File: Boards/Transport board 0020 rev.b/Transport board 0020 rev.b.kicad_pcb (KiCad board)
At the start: 2 copper layers, 165.9 x 187.4 mm, 84 parts, among them P1 CEC card edge connector large, U1 TR1602, U10 LM311, U11 LM741, U12 LM311, U13 AH5012, U14 Spare, U15 Spare, U2 6821, U3 DM8602N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

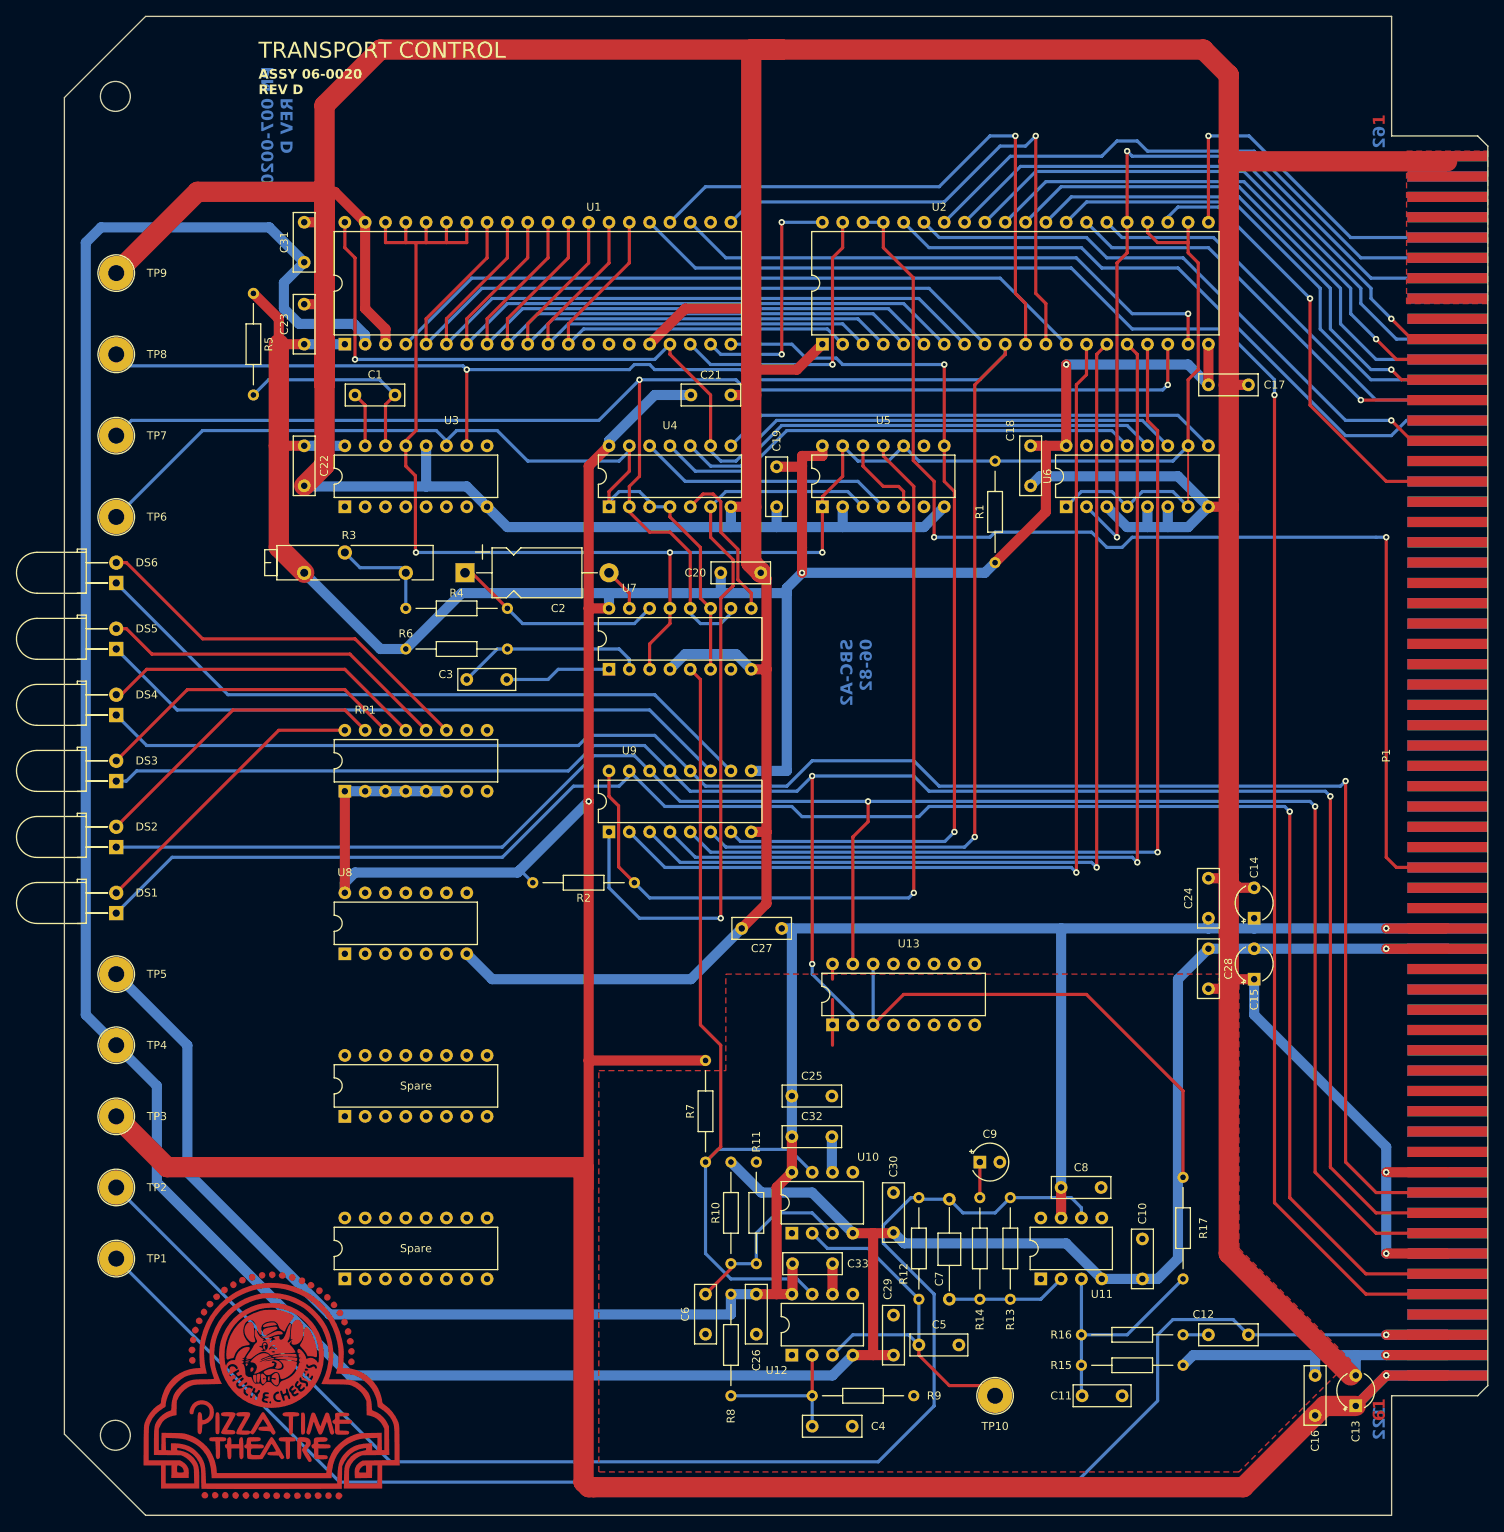
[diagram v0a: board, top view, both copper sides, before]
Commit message: Fix spelling errors with Transport
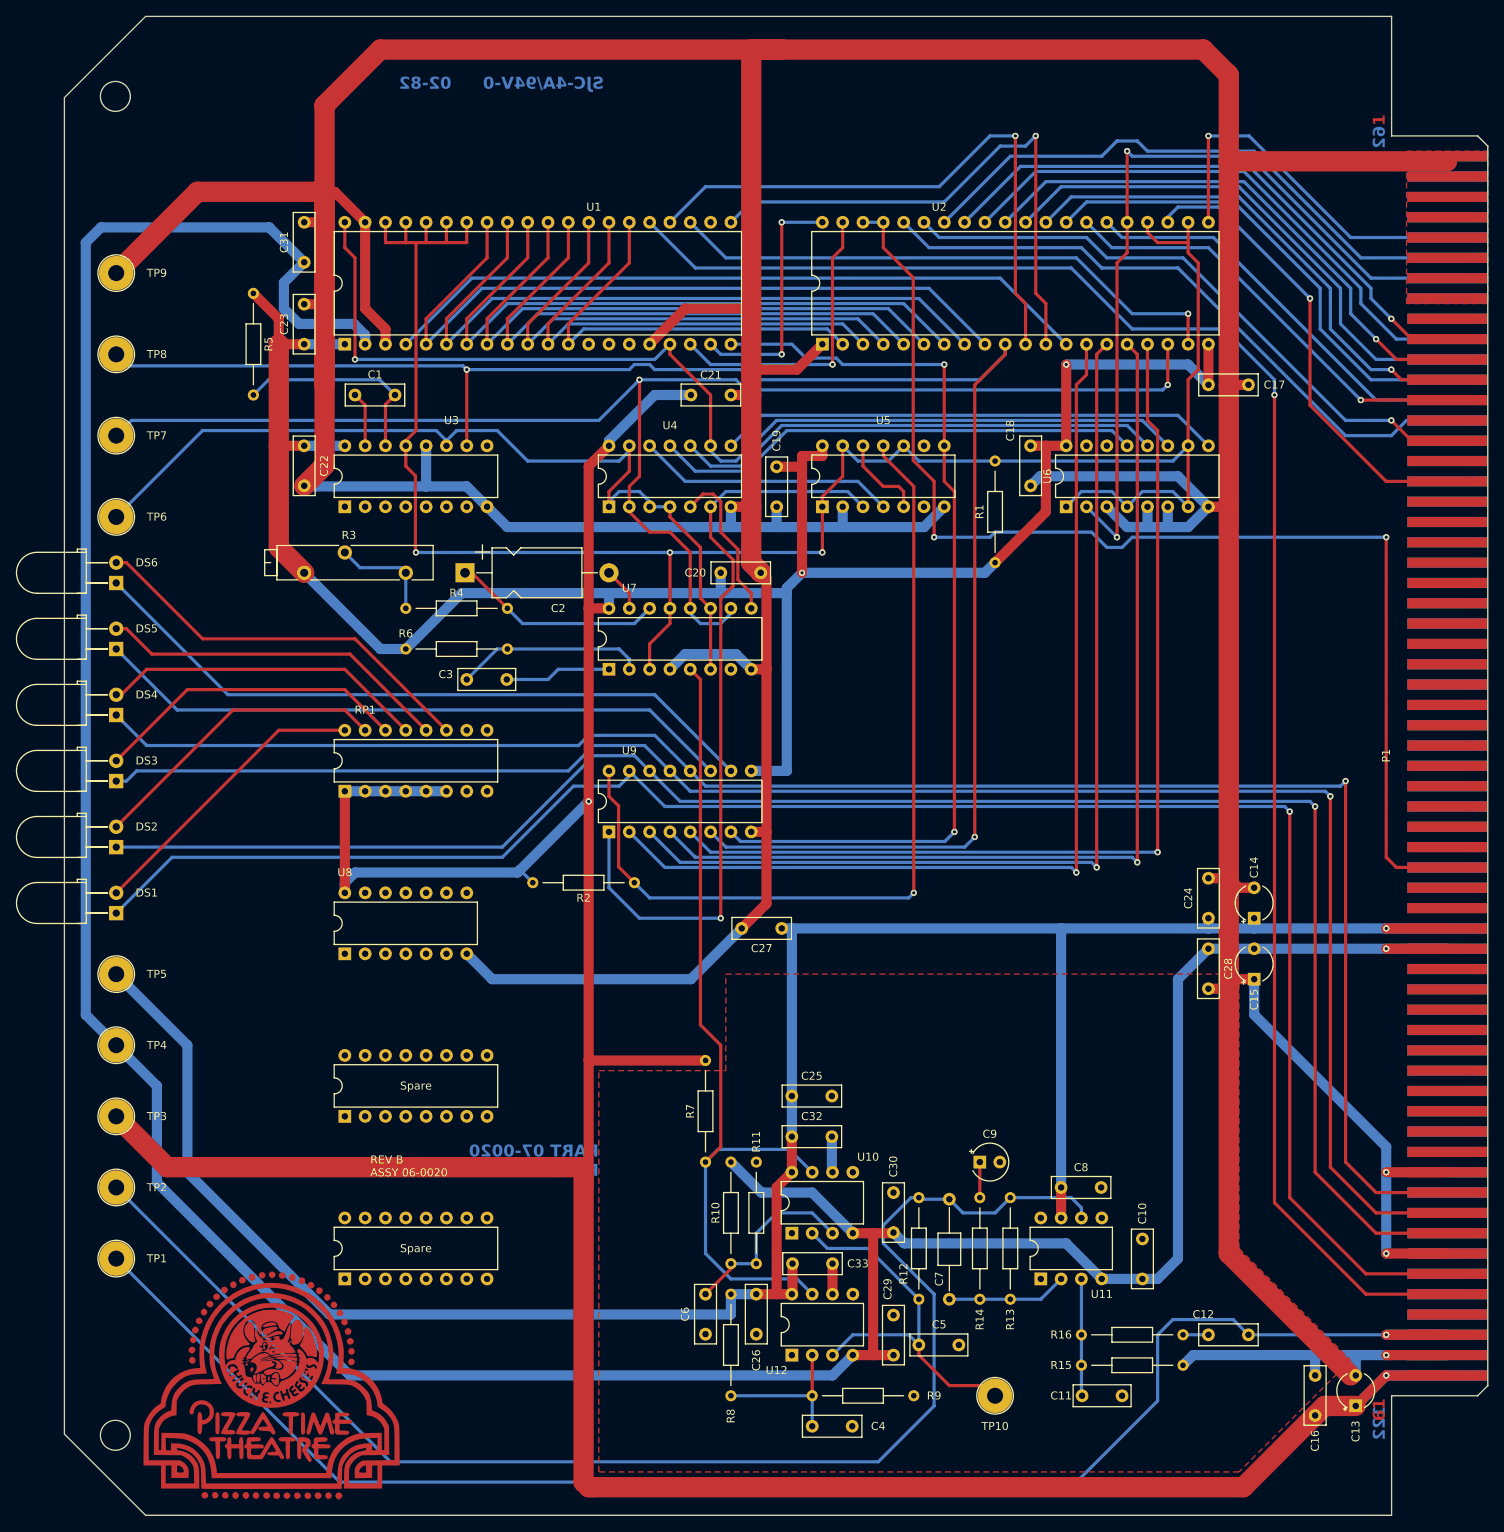
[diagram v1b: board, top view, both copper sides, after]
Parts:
- removed R17: 2.2K, Evan's parts:R_Axial_DIN0204_L3.6mm_D1.6mm_P12.7mm_Horizontal
- removed U13: AH5012, Package_DIP:DIP-16_W7.62mm
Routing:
- net Net-(R17-Pad2): track 63.7 -> 0.00 mm
- net R.W.: track 254.4 -> 219.6 mm, vias 3 -> 1
- net F.F.: track 243.7 -> 222.6 mm, vias 2 -> 1
- net Net-(U11-+): track 30.2 -> 14.6 mm
- net GND: track 911.2 -> 903.6 mm
- net PLAY: track 223.2 -> 220.6 mm
- net STOP: track 229.5 -> 228.4 mm
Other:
- board text added: "02-82"
- board text added: "PART 07-0020 REV B"
- board text added: "REV B ASSY 06-0020"
- board text added: "SJC-4A/94V-0"
- board text removed: "ASSY 06-0020 REV D"
- board text removed: "PN 007-0020 REV D"
- board text removed: "SBC-A2 06-82"
- board text removed: "TRANSPORT CONTROL"
